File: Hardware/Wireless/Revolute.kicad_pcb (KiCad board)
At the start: 4 copper layers, 19.8 x 20 mm, 57 parts, among them U1 BQ27441-G1, U2 nrf52833_qfn40, U3 AS5600, U4 AP2112K-3.3, U5 BQ24075RGT, U6 Button, X1 32.768 kHz, X2 32MHZ

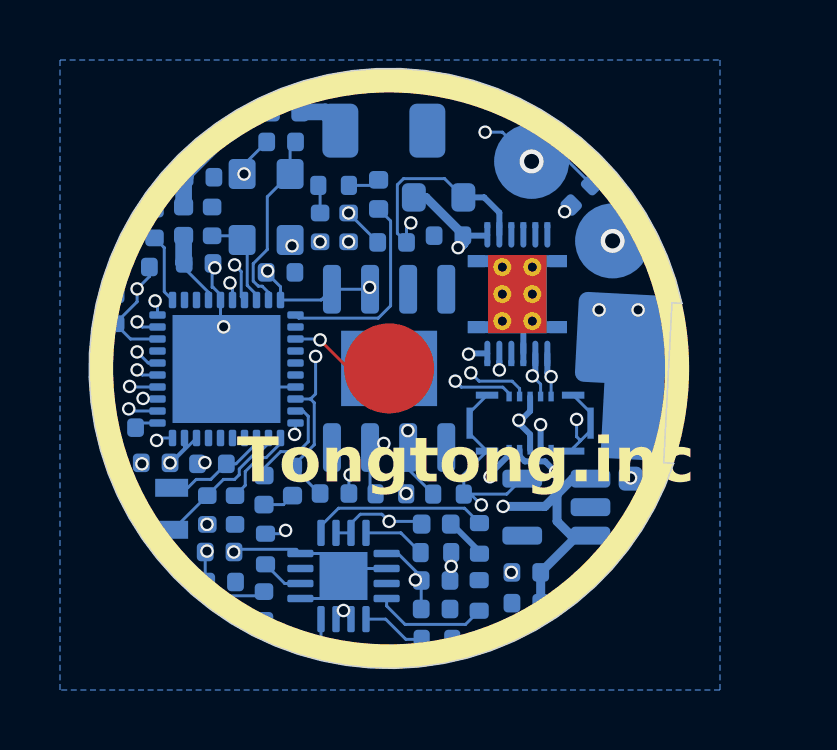
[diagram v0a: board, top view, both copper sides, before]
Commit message: fixed usb datapin issue
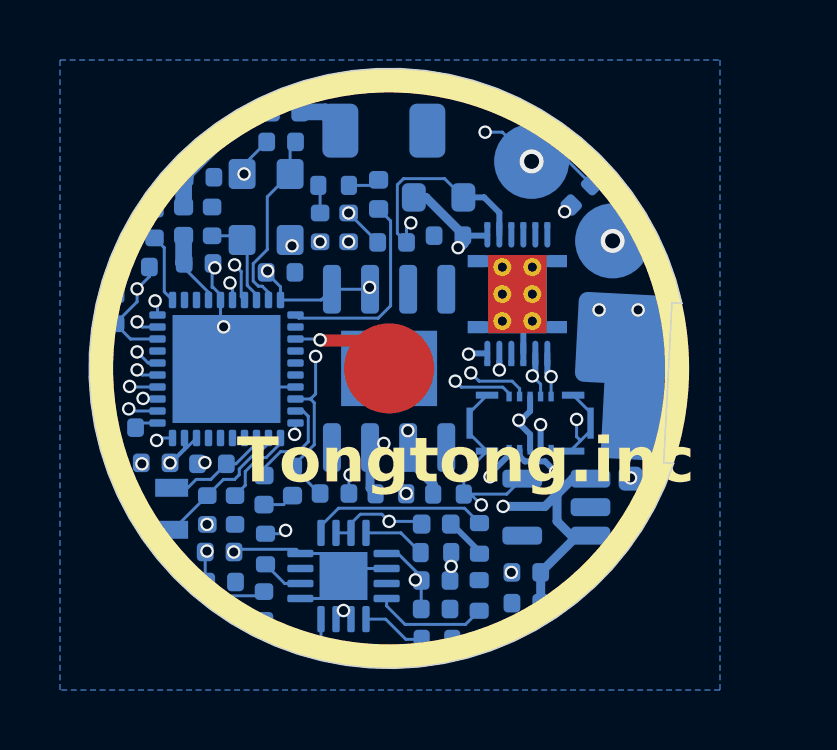
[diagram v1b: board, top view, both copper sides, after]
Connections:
- U2 pad 12: D+ -> D-
- U2 pad 13: D- -> D+
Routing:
- net D+: track 18.3 -> 16.9 mm
- net D-: track 14.3 -> 15.1 mm

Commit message: fixed debugger datapin board, connected dir and out of as5600 to mcu
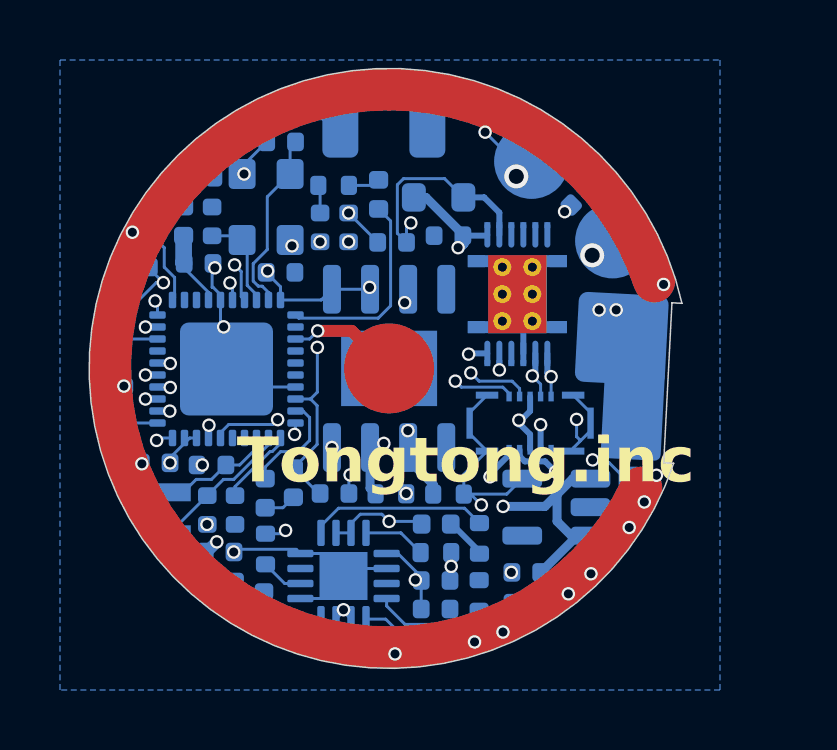
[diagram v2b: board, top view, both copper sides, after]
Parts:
- moved C8 0.90 mm to (162.2, 96.1), turned to -90 degrees
- moved X1 0.17 mm to (163.8, 99.8)
- moved L1 0.11 mm to (166.9, 99.2)
- moved L2 0.06 mm to (167.8, 98.8)
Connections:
- U2 pad 6: unconnected-(U2-P1.09-Pad6) -> DIR
- U2 pad 7: unconnected-(U2-P0.11-Pad7) -> ASOUT
- U3 pad 3: unconnected-(U3-OUT-Pad3) -> ASOUT
- U3 pad 8: unconnected-(U3-DIR-Pad8) -> DIR
- U5 pad 15: sysoff -> GND
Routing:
- net ASOUT: track 0.00 -> 9.51 mm, vias 0 -> 2
- net DIR: track 0.00 -> 4.46 mm, vias 0 -> 2
- net P0.15: track 23.7 -> 21.9 mm
- net RESET: track 20.2 -> 18.5 mm
- net D-: track 15.1 -> 13.6 mm
- net Batteryin: track 23.6 -> 22.6 mm
- net P0.17: track 21.6 -> 20.9 mm
- net swd: track 14.2 -> 13.5 mm

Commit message: updated gerbers
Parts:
- moved ? 0.08 mm to (179.0, 98.6)

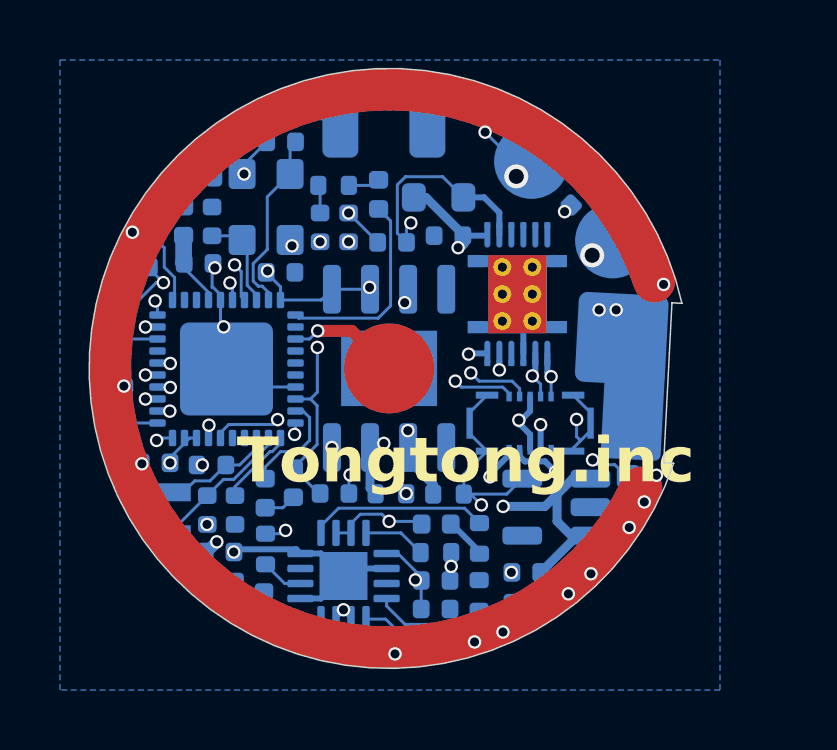
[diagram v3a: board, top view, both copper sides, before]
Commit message: revised wireless design
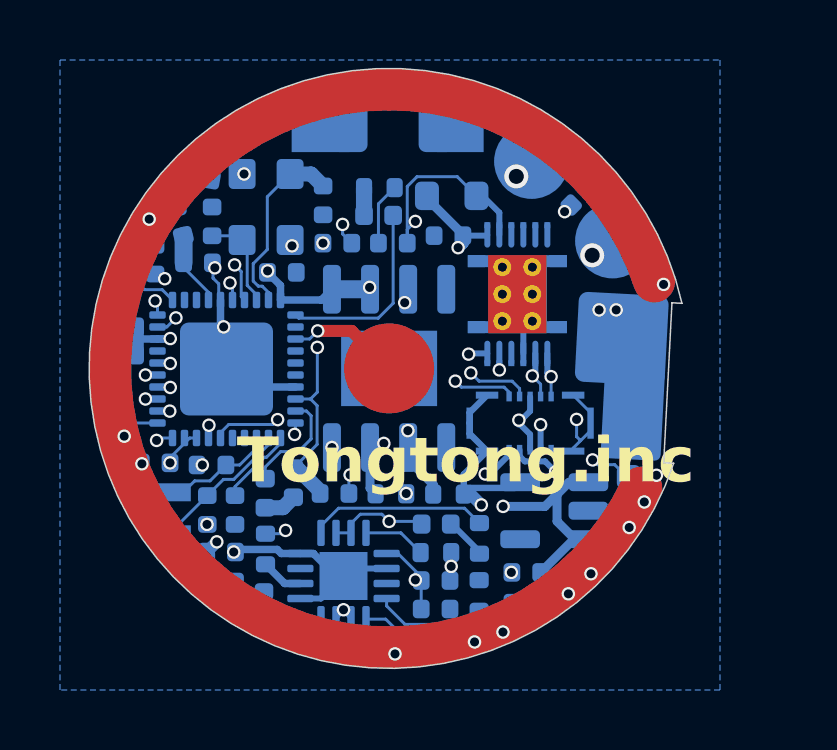
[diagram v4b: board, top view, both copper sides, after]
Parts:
- moved C9 5.60 mm to (163.2, 91.4)
- moved C16 2.40 mm to (168.8, 89.4), turned to 90 degrees
- moved C14 2.23 mm to (162.2, 92.2), turned to 90 degrees
- moved C1 2.04 mm to (162.1, 93.6)
- moved C7 1.54 mm to (162.1, 94.6), turned to 180 degrees
- moved R2 1.53 mm to (170.7, 89.0), turned to 180 degrees
- moved C8 0.70 mm to (162.2, 96.8), turned to 90 degrees
- moved D1 0.70 mm to (170.7, 89.9), turned to 0 degrees
- moved C18 0.65 mm to (169.3, 90.8), turned to 180 degrees
- moved R1 0.44 mm to (173.1, 89.2)
- moved AE1 0.36 mm to (171.1, 86.9)
- moved L4 0.33 mm to (167.2, 86.5), turned to 22 degrees
- moved R3 0.16 mm to (170.6, 104.4)
- moved U4 0.14 mm to (176.5, 99.7)
- moved L3 0.13 mm to (164.0, 90.1), turned to 104 degrees
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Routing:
- net GND: track 34.9 -> 29.8 mm, vias 26 -> 25
- net Net-(C19-Pad2): track 4.78 -> 0.00 mm
- net VDD_nRF: track 24.0 -> 21.5 mm
- net Net-(AE1-A): track 1.69 -> 0.00 mm
- net Net-(U2-DEC4): track 15.1 -> 13.5 mm
- net Net-(U2-DEC3): track 5.83 -> 4.99 mm
- net Batteryin: track 22.7 -> 22.0 mm
- net vBAT: track 22.2 -> 21.5 mm
- net swd: track 13.5 -> 13.0 mm

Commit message: implemented 4button design
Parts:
- added U10: Button, Library:SMDButton, F.Cu at (177.0, 95.0)
- added U8: Button, Library:SMDButton, F.Cu at (165.0, 95.0)
- added U9: Button, Library:SMDButton, F.Cu at (171.0, 89.0)
- U6: footprint Library:buttoncompliant -> Library:SMDButton
- moved U6 6.00 mm to (171.0, 101.0), turned to 180 degrees
- moved C13 0.21 mm to (163.0, 98.2)
- moved C3 0.09 mm to (165.0, 98.2)
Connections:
- U2 pad 33: Net-(U2-P0.28/AIN4) -> P0.28
- U2 pad 34: unconnected-(U2-P0.29/AIN5-Pad34) -> P0.29
- U2 pad 35: unconnected-(U2-P0.30/AIN6-Pad35) -> P0.30
- U2 pad 36: unconnected-(U2-P0.31/AIN7-Pad36) -> P0.31
- U6 pad 3: Net-(U2-P0.28/AIN4) -> P0.31
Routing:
- net P0.28: track 0.00 -> 9.39 mm, vias 0 -> 1
- net P0.30: track 0.00 -> 8.23 mm, vias 0 -> 1
- net P0.31: track 0.00 -> 6.95 mm, vias 0 -> 1
- net P0.29: track 0.00 -> 3.79 mm, vias 0 -> 1
- net Net-(U2-P0.28/AIN4): track 3.75 -> 0.00 mm, vias 1 -> 0
- net GND: track 29.8 -> 31.6 mm, vias 25 -> 26
- net Net-(U2-DEC4): track 13.5 -> 14.4 mm
- net swc: track 14.1 -> 14.6 mm
- added copper zone on F.Cu, net GND

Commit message: new gerbers
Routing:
- net Batteryin: track 22.0 -> 21.5 mm
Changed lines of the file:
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@@
   (segment (start 171.895 102.07) (end 171.875 102.05) (width 0.1) (layer "B.Cu") (net 3))
   (segment (start 175.325 96.825) (end 175.325 97.095) (width 0.2) (layer "B.Cu") (net 3))
-  (segment (start 167.985 93.325) (end 170.639264 93.325) (width 0.1) (layer "B.Cu") (net 4))
-  (segment (start 167.88 93.22) (end 167.985 93.325) (width 0.1) (layer "B.Cu") (net 4))
   (segment (start 171.135 92.829264) (end 171.135 89.9) (width 0.1) (layer "B.Cu") (net 4))
+  (segment (start 167.88 93.22) (end 168.46 93.22) (width 0.1) (layer "B.Cu") (net 4))
   (segment (start 170.639264 93.325) (end 171.135 92.829264) (width 0.1) (layer "B.Cu") (net 4))
+  (segment (start 168.565 93.325) (end 170.639264 93.325) (width 0.1) (layer "B.Cu") (net 4))
+  (segment (start 168.46 93.22) (end 168.565 93.325) (width 0.1) (layer "B.Cu") (net 4))
   (segment (start 170.165 89.9) (end 170.165 88.975) (width 0.54) (layer "B.Cu") (net 5))
   (via (at 163.199979 92.750054) (size 0.45) (drill 0.3) (layers "F.Cu" "B.Cu") (net 6))
@@
   (segment (start 173.9 90.1) (end 174.73 89.27) (width 0.4) (layer "In2.Cu") (net 11))
   (segment (start 174.675 89.806579) (end 174.675 90.55) (width 0.2) (layer "B.Cu") (net 11))
-  (segment (start 171.605 90.825) (end 171.605 90.37) (width 0.1) (layer "B.Cu") (net 11))
-  (segment (start 171.929739 88.61) (end 173.27383 88.61) (width 0.1) (layer "B.Cu") (net 11))
-  (segment (start 171.605 90.825) (end 171.605 88.934739) (width 0.1) (layer "B.Cu") (net 11))
+  (segment (start 173.22383 88.56) (end 173.911772 89.247942) (width 0.2) (layer "B.Cu") (net 11))
+  (segment (start 171.655 88.795) (end 171.89 88.56) (width 0.2) (layer "B.Cu") (net 11))
+  (segment (start 171.605 90.825) (end 171.655 90.775) (width 0.2) (layer "B.Cu") (net 11))
   (segment (start 178.716087 94.711271) (end 178.716087 93.646926) (width 0.2) (layer "B.Cu") (net 11))
   (segment (start 178.57 93.05) (end 178.716087 93.196087) (width 0.2) (layer "B.Cu") (net 11))
+  (segment (start 171.875 90.1) (end 171.655 90.1) (width 0.2) (layer "B.Cu") (net 11))
   (segment (start 178.716087 93.646926) (end 179.171757 93.191256) (width 0.2) (layer "B.Cu") (net 11))
   (segment (start 174.116363 89.247942) (end 174.675 89.806579) (width 0.2) (layer "B.Cu") (net 11))
@@
   (segment (start 178.716087 93.766087) (end 178 93.05) (width 0.2) (layer "B.Cu") (net 11))
   (segment (start 174.275 94.5) (end 173.675 94.5) (width 0.2) (layer "B.Cu") (net 11))
-  (segment (start 173.27383 88.61) (end 173.911772 89.247942) (width 0.1) (layer "B.Cu") (net 11))
+  (segment (start 171.655 90.1) (end 171.655 88.795) (width 0.2) (layer "B.Cu") (net 11))
   (segment (start 173.675 94.5) (end 173.65 94.525) (width 0.2) (layer "B.Cu") (net 11))
+  (segment (start 171.89 88.56) (end 173.22383 88.56) (width 0.2) (layer "B.Cu") (net 11))
   (segment (start 178.716087 94.711271) (end 178.716087 93.766087) (width 0.2) (layer "B.Cu") (net 11))
+  (segment (start 171.655 90.775) (end 171.655 90.1) (width 0.2) (layer "B.Cu") (net 11))
   (segment (start 178.716087 93.196087) (end 178.716087 94.711271) (width 0.2) (layer "B.Cu") (net 11))
-  (segment (start 171.605 90.37) (end 171.875 90.1) (width 0.1) (layer "B.Cu") (net 11))
   (segment (start 178 93.05) (end 178 93) (width 0.2) (layer "B.Cu") (net 11))
-  (segment (start 171.605 88.934739) (end 171.929739 88.61) (width 0.1) (layer "B.Cu") (net 11))
   (segment (start 173.055 100.19) (end 173.095805 100.19) (width 0.2) (layer "B.Cu") (net 12))
   (segment (start 174.011227 101.105422) (end 174.011227 101.176601) (width 0.2) (layer "B.Cu") (net 12))
